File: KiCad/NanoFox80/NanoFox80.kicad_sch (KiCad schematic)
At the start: 53 parts, among them J101 Conn_01x02, J102 Conn_01x02, J111 DB9 Female, J112 Conn_01x02, J113 Conn_01x02, J115 Conn_01x02, P101 ISP/PDI, Q101 BSS84W-7-F, Q102 BSS138W-7-F, SW101 SW_SPST, U101 MC74VHC1G125, U102 LP2985-3.3, U104 LP2985-3.3, U105 AVR128DA28, X101 SIT1566AC TCO

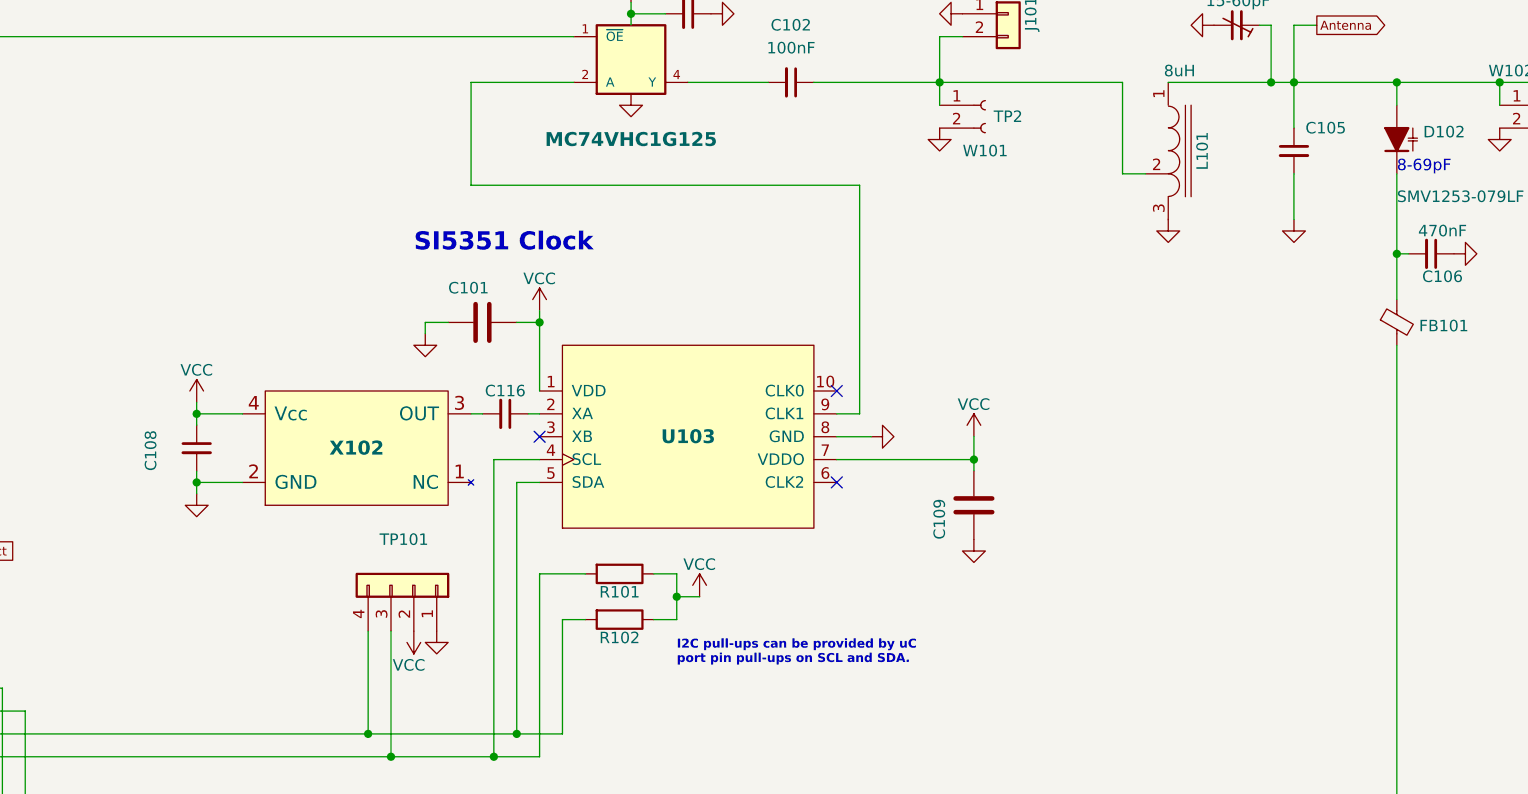
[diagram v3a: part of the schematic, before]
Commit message: Development
o Changes to footprints in schematic
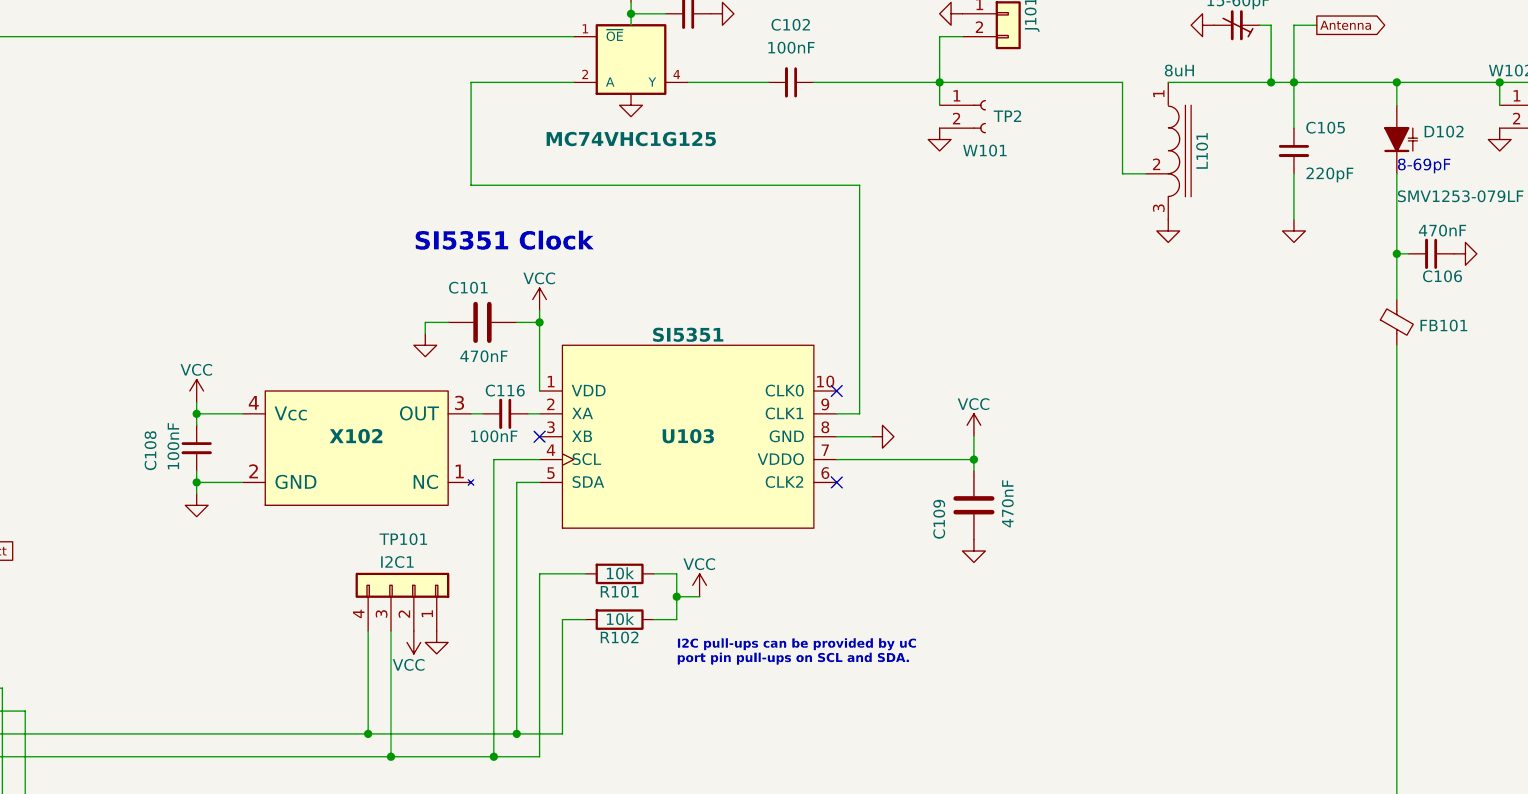
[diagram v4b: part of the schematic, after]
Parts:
- C101, C109: value (none) -> 470nF; footprint (none) -> Capacitor_SMD:C_0805_2012Metric
- C105: value (none) -> 220pF; footprint (none) -> Capacitor_SMD:C_0805_2012Metric
- C108, C116: value (none) -> 100nF; footprint (none) -> Capacitor_SMD:C_0805_2012Metric
- D103, D104: value (none) -> ESD9B5.0ST5G_1; footprint (none) -> Diode_SMD:D_0603_1608Metric
- MOD1: footprint (none) -> Connector_PinHeader_2.54mm:PinHeader_1x04_P2.54mm_Vertical
- R101, R102: value (none) -> 10k; footprint (none) -> Resistor_SMD:R_0805_2012Metric
- TP101: value (none) -> I2C1; footprint (none) -> Connector_PinHeader_2.54mm:PinHeader_1x04_P2.54mm_Vertical
- U103: value (none) -> SI5351; footprint (none) -> Package_SO:MSOP-10_3x3mm_P0.5mm
- X102: Digi-Key Part No. 2780-I537-2O7-25.000MHZCT-ND -> 1664-1273-1-ND; Link <a href="https://www.digikey.com/products/en?keywords=2780-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 -> <a href="https://www.digikey.com/products/en?keywords=1664-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; Manufacturer Abracon LLC -> Taitien; Manufacturer PN I537-2O7-25.000 MHZ -> TXETCLSANF-25.000000
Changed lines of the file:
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@@
       (effects (font (size 1.27 1.27)) (justify left))
     )
-    (property "Value" "" (id 1) (at 133.35 82.55 90)
-      (effects (font (size 1.27 1.27)) (justify left))
-    )
-    (property "Footprint" "" (id 2) (at 137.16 85.09 0)
+    (property "Value" "I2C1" (id 1) (at 133.35 82.55 90)
+      (effects (font (size 1.27 1.27)) (justify left))
+    )
+    (property "Footprint" "Connector_PinHeader_2.54mm:PinHeader_1x04_P2.54mm_Vertical" (id 2) (at 137.16 85.09 0)
       (effects (font (size 1.27 1.27)) hide)
     )
@@
       (effects (font (size 1.524 1.524) bold))
     )
-    (property "Value" "" (id 1) (at 167.64 57.3088 0)
+    (property "Value" "SI5351" (id 1) (at 167.64 57.3088 0)
       (effects (font (size 1.524 1.524) bold))
     )
-    (property "Footprint" "" (id 2) (at 167.64 68.58 0)
+    (property "Footprint" "Package_SO:MSOP-10_3x3mm_P0.5mm" (id 2) (at 167.64 68.58 0)
       (effects (font (size 1.27 1.27)) hide)
     )
@@
     (in_bom yes) (on_board yes)
     (property "Reference" "R102" (id 0) (at 160.02 90.932 90))
-    (property "Value" "" (id 1) (at 160.02 88.9 90))
-    (property "Footprint" "" (id 2) (at 160.02 87.122 0)
+    (property "Value" "10k" (id 1) (at 160.02 88.9 90))
+    (property "Footprint" "Resistor_SMD:R_0805_2012Metric" (id 2) (at 160.02 87.122 0)
       (effects (font (size 1.27 1.27)) hide)
     )
@@
       (effects (font (size 1.27 1.27)) (justify left))
     )
-    (property "Value" "" (id 1) (at 203.2 78.74 90)
-      (effects (font (size 1.27 1.27)) (justify left))
-    )
-    (property "Footprint" "" (id 2) (at 200.3552 80.01 0)
+    (property "Value" "470nF" (id 1) (at 203.2 78.74 90)
+      (effects (font (size 1.27 1.27)) (justify left))
+    )
+    (property "Footprint" "Capacitor_SMD:C_0805_2012Metric" (id 2) (at 200.3552 80.01 0)
       (effects (font (size 1.27 1.27)) hide)
     )
@@
       (effects (font (size 1.27 1.27)) (justify left))
     )
-    (property "Value" "" (id 1) (at 120.777 131.5466 90)
+    (property "Value" "ESD9B5.0ST5G_1" (id 1) (at 120.777 131.5466 90)
       (effects (font (size 1.27 1.27)) (justify right) hide)
     )
-    (property "Footprint" "" (id 2) (at 121.92 129.54 0)
+    (property "Footprint" "Diode_SMD:D_0603_1608Metric" (id 2) (at 121.92 129.54 0)
       (effects (font (size 1.27 1.27)) hide)
     )
@@
       (effects (font (size 1.27 1.27)) (justify left))
     )
-    (property "Value" "" (id 1) (at 120.777 144.2466 90)
+    (property "Value" "ESD9B5.0ST5G_1" (id 1) (at 120.777 144.2466 90)
       (effects (font (size 1.27 1.27)) (justify right) hide)
     )
-    (property "Footprint" "" (id 2) (at 121.92 142.24 0)
+    (property "Footprint" "Diode_SMD:D_0603_1608Metric" (id 2) (at 121.92 142.24 0)
       (effects (font (size 1.27 1.27)) hide)
     )
@@
       (effects (font (size 1.27 1.27)) (justify left))
     )
-    (property "Value" "" (id 1) (at 142.24 59.69 90)
-      (effects (font (size 1.27 1.27)) (justify left))
-    )
-    (property "Footprint" "" (id 2) (at 140.97 56.8452 0)
+    (property "Value" "470nF" (id 1) (at 142.24 59.69 90)
+      (effects (font (size 1.27 1.27)) (justify left))
+    )
+    (property "Footprint" "Capacitor_SMD:C_0805_2012Metric" (id 2) (at 140.97 56.8452 0)
       (effects (font (size 1.27 1.27)) hide)
     )
@@
     (in_bom yes) (on_board yes)
     (property "Reference" "R101" (id 0) (at 160.02 85.852 90))
-    (property "Value" "" (id 1) (at 160.02 83.82 90))
-    (property "Footprint" "" (id 2) (at 160.02 82.042 0)
+    (property "Value" "10k" (id 1) (at 160.02 83.82 90))
+    (property "Footprint" "Resistor_SMD:R_0805_2012Metric" (id 2) (at 160.02 82.042 0)
       (effects (font (size 1.27 1.27)) hide)
     )
@@
   (symbol (lib_id "Oscillator:ASTX-H11") (at 130.81 69.85 0) (unit 1)
     (in_bom yes) (on_board yes)
-    (property "Reference" "X102" (id 0) (at 130.81 69.85 0)
+    (property "Reference" "X102" (id 0) (at 130.81 68.58 0)
       (effects (font (size 1.5494 1.5494) bold))
     )
-    (property "Value" "" (id 1) (at 130.81 62.3829 0)
+    (property "Value" "" (id 1) (at 130.81 71.12 0)
       (effects (font (size 1.5494 1.5494) bold))
     )
@@
       (effects (font (size 1.524 1.524)) hide)
     )
-    (property "Digi-Key Part No." "2780-I537-2O7-25.000MHZCT-ND" (id 4) (at 130.81 69.85 0)
-      (effects (font (size 1.27 1.27)) hide)
-    )
-    (property "Link" "<a href=\"https://www.digikey.com/products/en?keywords=2780-I537-2O7-25.000MHZCT-ND\">Link</a>" (id 5) (at 130.81 69.85 0)
+    (property "Digi-Key Part No." "1664-1273-1-ND" (id 4) (at 130.81 69.85 0)
+      (effects (font (size 1.27 1.27)) hide)
+    )
+    (property "Link" "<a href=\"https://www.digikey.com/products/en?keywords=1664-1273-1-ND\">Link</a>" (id 5) (at 130.81 69.85 0)
       (effects (font (size 1.524 1.524)) hide)
     )
-    (property "Manufacturer" "Abracon LLC" (id 6) (at 130.81 69.85 0)
-      (effects (font (size 1.27 1.27)) hide)
-    )
-    (property "Manufacturer PN" "I537-2O7-25.000 MHZ" (id 7) (at 130.81 69.85 0)
-      (effects (font (size 1.27 1.27)) hide)
-    )
-    (property "Description" "XTAL OSC TCXO 25MHZ CLPSNW" (id 8) (at 130.81 69.85 0)
+    (property "Manufacturer" "Taitien" (id 6) (at 130.81 69.85 0)
+      (effects (font (size 1.27 1.27)) hide)
+    )
+    (property "Manufacturer PN" "TXETCLSANF-25.000000" (id 7) (at 130.81 69.85 0)
+      (effects (font (size 1.27 1.27)) hide)
+    )
+    (property "Description" "XTAL OSC TCXO 25.0000MHZ SNWV" (id 8) (at 130.81 69.85 0)
       (effects (font (size 1.27 1.27)) hide)
     )
@@
     (in_bom yes) (on_board yes)
     (property "Reference" "C116" (id 0) (at 147.32 63.5 90))
-    (property "Value" "" (id 1) (at 146.05 68.58 90))
-    (property "Footprint" "" (id 2) (at 147.32 66.04 0)
+    (property "Value" "100nF" (id 1) (at 146.05 68.58 90))
+    (property "Footprint" "Capacitor_SMD:C_0805_2012Metric" (id 2) (at 147.32 66.04 0)
       (effects (font (size 1.27 1.27)) hide)
     )
@@
       (effects (font (size 1.27 1.27)) (justify left))
     )
-    (property "Value" "" (id 1) (at 110.49 72.39 90)
-      (effects (font (size 1.27 1.27)) (justify left))
-    )
-    (property "Footprint" "" (id 2) (at 113.03 69.85 0)
+    (property "Value" "100nF" (id 1) (at 110.49 72.39 90)
+      (effects (font (size 1.27 1.27)) (justify left))
+    )
+    (property "Footprint" "Capacitor_SMD:C_0805_2012Metric" (id 2) (at 113.03 69.85 0)
       (effects (font (size 1.27 1.27)) hide)
     )
@@
       (effects (font (size 1.27 1.27)) (justify left))
     )
-    (property "Value" "" (id 1) (at 236.22 39.37 0)
-      (effects (font (size 1.27 1.27)) (justify left))
-    )
-    (property "Footprint" "" (id 2) (at 234.95 36.83 0)
+    (property "Value" "220pF" (id 1) (at 236.22 39.37 0)
+      (effects (font (size 1.27 1.27)) (justify left))
+    )
+    (property "Footprint" "Capacitor_SMD:C_0805_2012Metric" (id 2) (at 234.95 36.83 0)
       (effects (font (size 1.27 1.27)) hide)
     )
@@
       (effects (font (size 1.27 1.27)) (justify left))
     )
-    (property "Footprint" "" (id 2) (at 153.67 181.61 0)
+    (property "Footprint" "Connector_PinHeader_2.54mm:PinHeader_1x04_P2.54mm_Vertical" (id 2) (at 153.67 181.61 0)
       (effects (font (size 1.27 1.27)) hide)
     )
@@
     )
     (path "/822d344f-208c-4e81-9deb-9412c3521d88"
-      (reference "X102") (unit 1) (value "ASTX-H11") (footprint "Crystal:Crystal_SMD_Abracon_ABM3C-4Pin_5.0x3.2mm")
-    )
-  )
+      (reference "X102") (unit 1) (value "25 MHz") (footprint "Crystal:Crystal_SMD_TXETCLSANF-4Pin")
+    )
+  )

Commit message: Development
o Footprint edits
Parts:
- MOD1: value AdaFruit Charger -> (none); footprint Connector_PinHeader_2.54mm:PinHeader_1x04_P2.54mm_Vertical -> (none); Digi-Key Part No. (none) -> 1528-1833-ND; Link (none) -> https://www.digikey.com/en/products/detail/adafruit-industr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; Manufacturer (none) -> AdaFruit; Manufacturer PN (none) -> Product ID: 1904
- X102: value (none) -> 25 MHz; footprint (none) -> Crystal:Crystal_SMD_TXETCLSANF-4Pin
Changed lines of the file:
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@@
       (effects (font (size 1.5494 1.5494) bold))
     )
-    (property "Value" "" (id 1) (at 130.81 71.12 0)
+    (property "Value" "25 MHz" (id 1) (at 130.81 71.12 0)
       (effects (font (size 1.5494 1.5494) bold))
     )
-    (property "Footprint" "" (id 2) (at 130.81 69.85 0)
+    (property "Footprint" "Crystal:Crystal_SMD_TXETCLSANF-4Pin" (id 2) (at 130.81 69.85 0)
       (effects (font (size 1.524 1.524)) hide)
     )
@@
       (effects (font (size 1.27 1.27)) (justify left))
     )
-    (property "Value" "AdaFruit Charger" (id 1) (at 155.702 184.5822 0)
-      (effects (font (size 1.27 1.27)) (justify left))
-    )
-    (property "Footprint" "Connector_PinHeader_2.54mm:PinHeader_1x04_P2.54mm_Vertical" (id 2) (at 153.67 181.61 0)
+    (property "Value" "" (id 1) (at 155.702 184.5822 0)
+      (effects (font (size 1.27 1.27)) (justify left))
+    )
+    (property "Footprint" "" (id 2) (at 153.67 181.61 0)
       (effects (font (size 1.27 1.27)) hide)
     )
@@
       (effects (font (size 1.27 1.27)) hide)
     )
+    (property "Digi-Key Part No." "1528-1833-ND" (id 4) (at 153.67 181.61 0)
+      (effects (font (size 1.27 1.27)) hide)
+    )
+    (property "Manufacturer" "AdaFruit" (id 5) (at 153.67 181.61 0)
+      (effects (font (size 1.27 1.27)) hide)
+    )
+    (property "Manufacturer PN" "Product ID: 1904" (id 6) (at 153.67 181.61 0)
+      (effects (font (size 1.27 1.27)) hide)
+    )
+    (property "Description" "LI-ION LI-POLYMER CHARGER BOARD" (id 7) (at 153.67 181.61 0)
+      (effects (font (size 1.27 1.27)) hide)
+    )
+    (property "Link" "https://www.digikey.com/en/products/detail/adafruit-industries-llc/1904/5054545" (id 8) (at 153.67 181.61 0)
+      (effects (font (size 1.27 1.27)) hide)
+    )

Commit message: Development
o Fixes to errors in schematic and PCB
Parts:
- MOD1: value (none) -> AdaFruit Charger; footprint (none) -> Connector_PinHeader_2.54mm:PinHeader_1x04_P2.54mm_Vertical
- U101: value MC74VHC1G125 -> (none); footprint Package_TO_SOT_SMD:TSOT-23-5 -> (none)
- U104: value LP2985-3.3 -> (none); footprint Package_TO_SOT_SMD:SOT-23-5 -> (none)
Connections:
- net GND: no longer C101.1, C108.1, C109.1, C111.2, C117.2, R101.1, R102.1, TP101.2 (Pin_2), U101.5 (VCC), U103.1 (VDD), U103.7 (VDDO), U104.5 (VOUT), X102.4 (Vcc)
- new net VCC: C101.1, C108.1, C109.1, C111.2, C117.2, R101.1, R102.1, TP101.2 (Pin_2), U101.5 (VCC), U103.1 (VDD), U103.7 (VDDO), U104.5 (VOUT), X102.4 (Vcc)

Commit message: Development
PCB Changes
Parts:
- U101: value (none) -> MC74VHC1G125; footprint (none) -> Package_TO_SOT_SMD:TSOT-23-5
- U104: value (none) -> LP2985-3.3; footprint (none) -> Package_TO_SOT_SMD:SOT-23-5
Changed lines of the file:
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@@
       (effects (font (size 1.27 1.27)) hide)
     )
-    (property "Value" "" (id 1) (at 116.84 171.6842 0))
+    (property "Value" "VDD" (id 1) (at 116.84 171.6842 0))
     (property "Footprint" "" (id 2) (at 116.84 175.26 0)
       (effects (font (size 1.27 1.27)) hide)
@@
       (effects (font (size 1.54 1.54) bold))
     )
-    (property "Value" "" (id 1) (at 91.44 190.5 0)
+    (property "Value" "LP2985-3.3" (id 1) (at 91.44 190.5 0)
       (effects (font (size 1.54 1.54) bold))
     )
-    (property "Footprint" "" (id 2) (at 102.87 174.625 0)
+    (property "Footprint" "Package_TO_SOT_SMD:SOT-23-5" (id 2) (at 102.87 174.625 0)
       (effects (font (size 1.27 1.27)) hide)
     )
@@
       (effects (font (size 1.54 1.54) bold))
     )
-    (property "Value" "" (id 1) (at 161.29 35.56 0)
+    (property "Value" "MC74VHC1G125" (id 1) (at 161.29 35.56 0)
       (effects (font (size 1.54 1.54) bold))
     )
-    (property "Footprint" "" (id 2) (at 161.29 26.67 0)
-      (effects (font (size 1.27 1.27)) hide)
-    )
+    (property "Footprint" "Package_TO_SOT_SMD:TSOT-23-5" (id 2) (at 161.29 26.67 0)
+      (effects (font (size 1.27 1.27)) hide)
+    )
